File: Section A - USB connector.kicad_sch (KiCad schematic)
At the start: 5 parts, among them J2 USB4135-GF-A_REVA

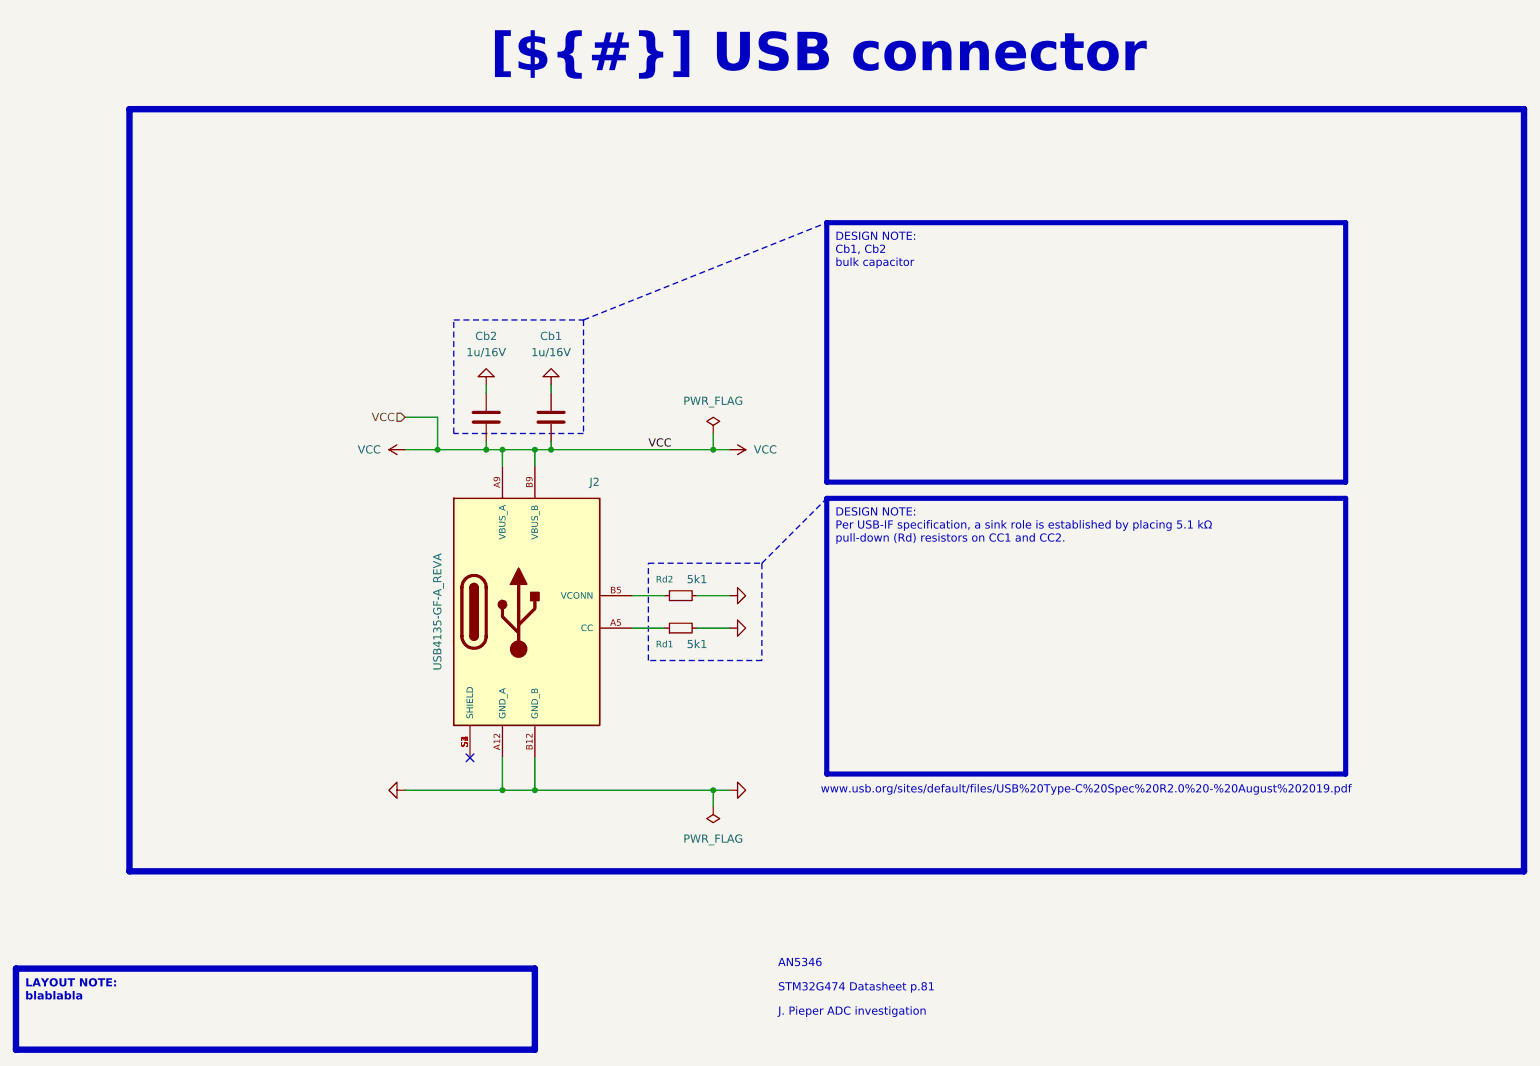
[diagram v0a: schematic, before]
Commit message: [CFG] Configuration update, added bom information fields
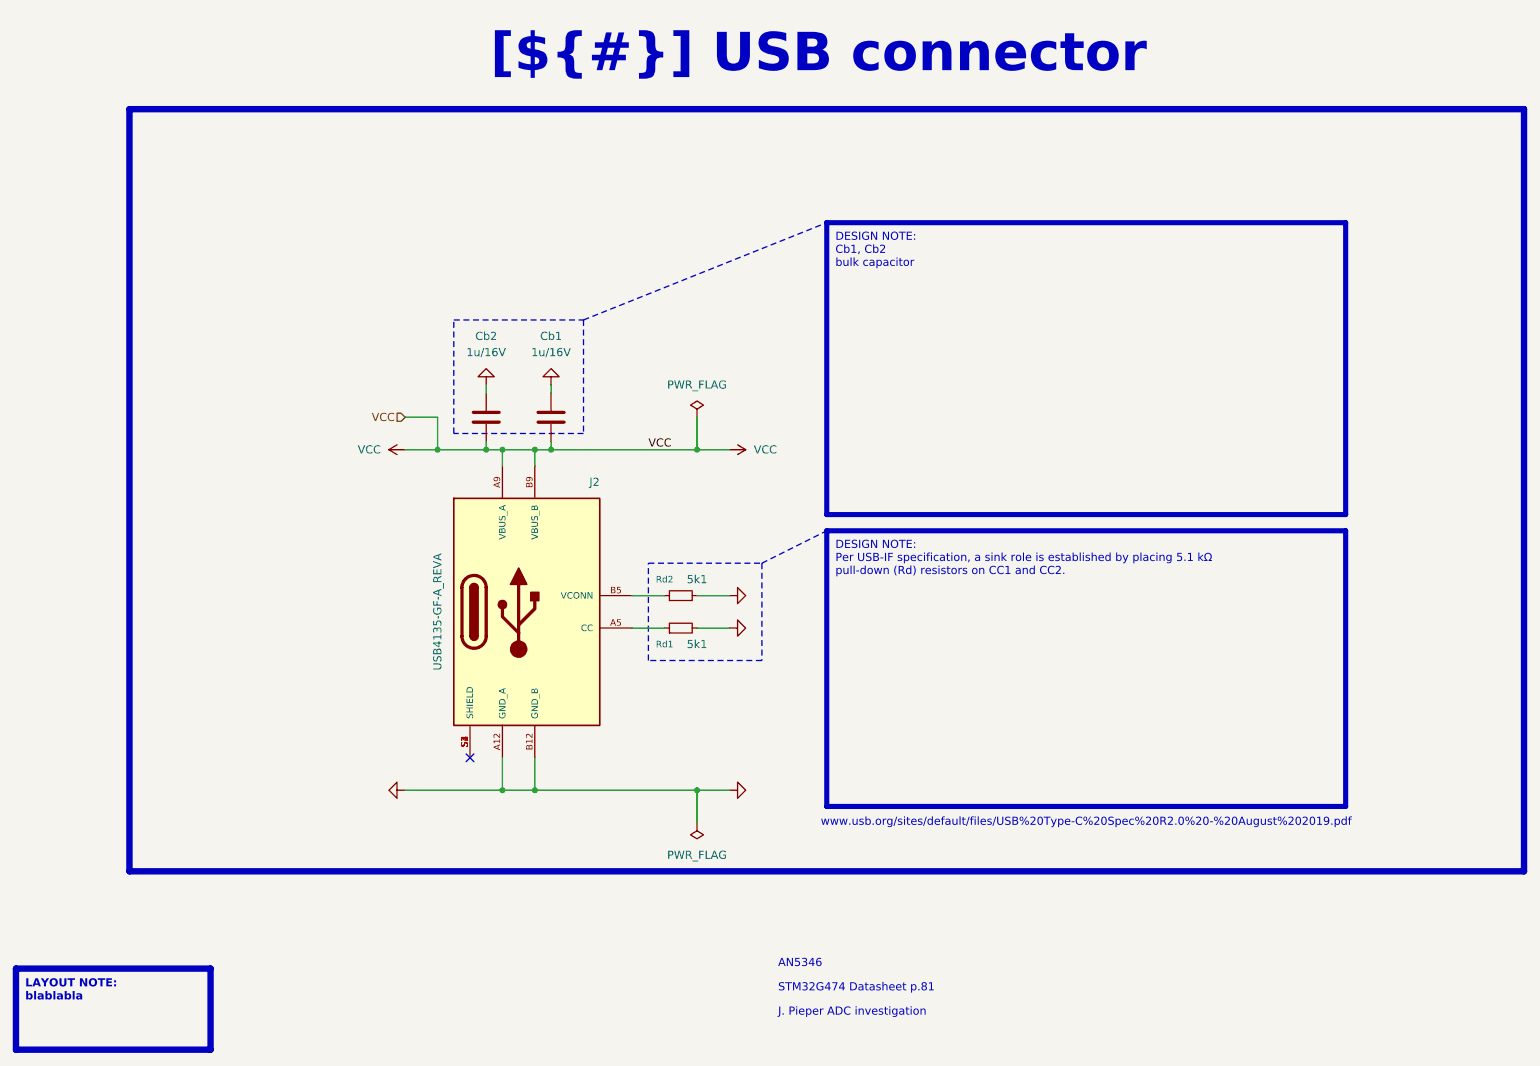
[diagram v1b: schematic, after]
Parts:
- Cb1, Cb2: BOM_INFO (none) -> TME have; BOM_STATUS (none) -> OK

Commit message: bom update, qr-code added
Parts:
- Cb1, Cb2: BOM_INFO TME have -> TME BOX
- J2: BOM_INFO (none) -> TME BOX; BOM_STATUS (none) -> OK
- Rd1, Rd2: BOM_INFO (none) -> TME BOX 25.06.2025; BOM_STATUS (none) -> OK
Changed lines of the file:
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@@
 			)
 		)
-		(property "BOM_INFO" ""
+		(property "BOM_INFO" "TME BOX 25.06.2025"
 			(at 127 104.14 90)
 			(effects
@@
 			)
 		)
-		(property "BOM_STATUS" ""
+		(property "BOM_STATUS" "OK"
 			(at 127 104.14 90)
 			(effects
@@
 			)
 		)
-		(property "BOM_INFO" "TME have"
+		(property "BOM_INFO" "TME BOX"
 			(at 106.68 76.2 0)
 			(effects
@@
 			)
 		)
-		(property "BOM_INFO" ""
+		(property "BOM_INFO" "TME BOX"
 			(at 101.6 106.68 0)
 			(effects
@@
 			)
 		)
-		(property "BOM_STATUS" ""
+		(property "BOM_STATUS" "OK"
 			(at 101.6 106.68 0)
 			(effects
@@
 			)
 		)
-		(property "BOM_INFO" "TME have"
+		(property "BOM_INFO" "TME BOX"
 			(at 96.52 76.2 0)
 			(effects
@@
 			)
 		)
-		(property "BOM_INFO" ""
+		(property "BOM_INFO" "TME BOX 25.06.2025"
 			(at 127 109.22 90)
 			(effects
@@
 			)
 		)
-		(property "BOM_STATUS" ""
+		(property "BOM_STATUS" "OK"
 			(at 127 109.22 90)
 			(effects

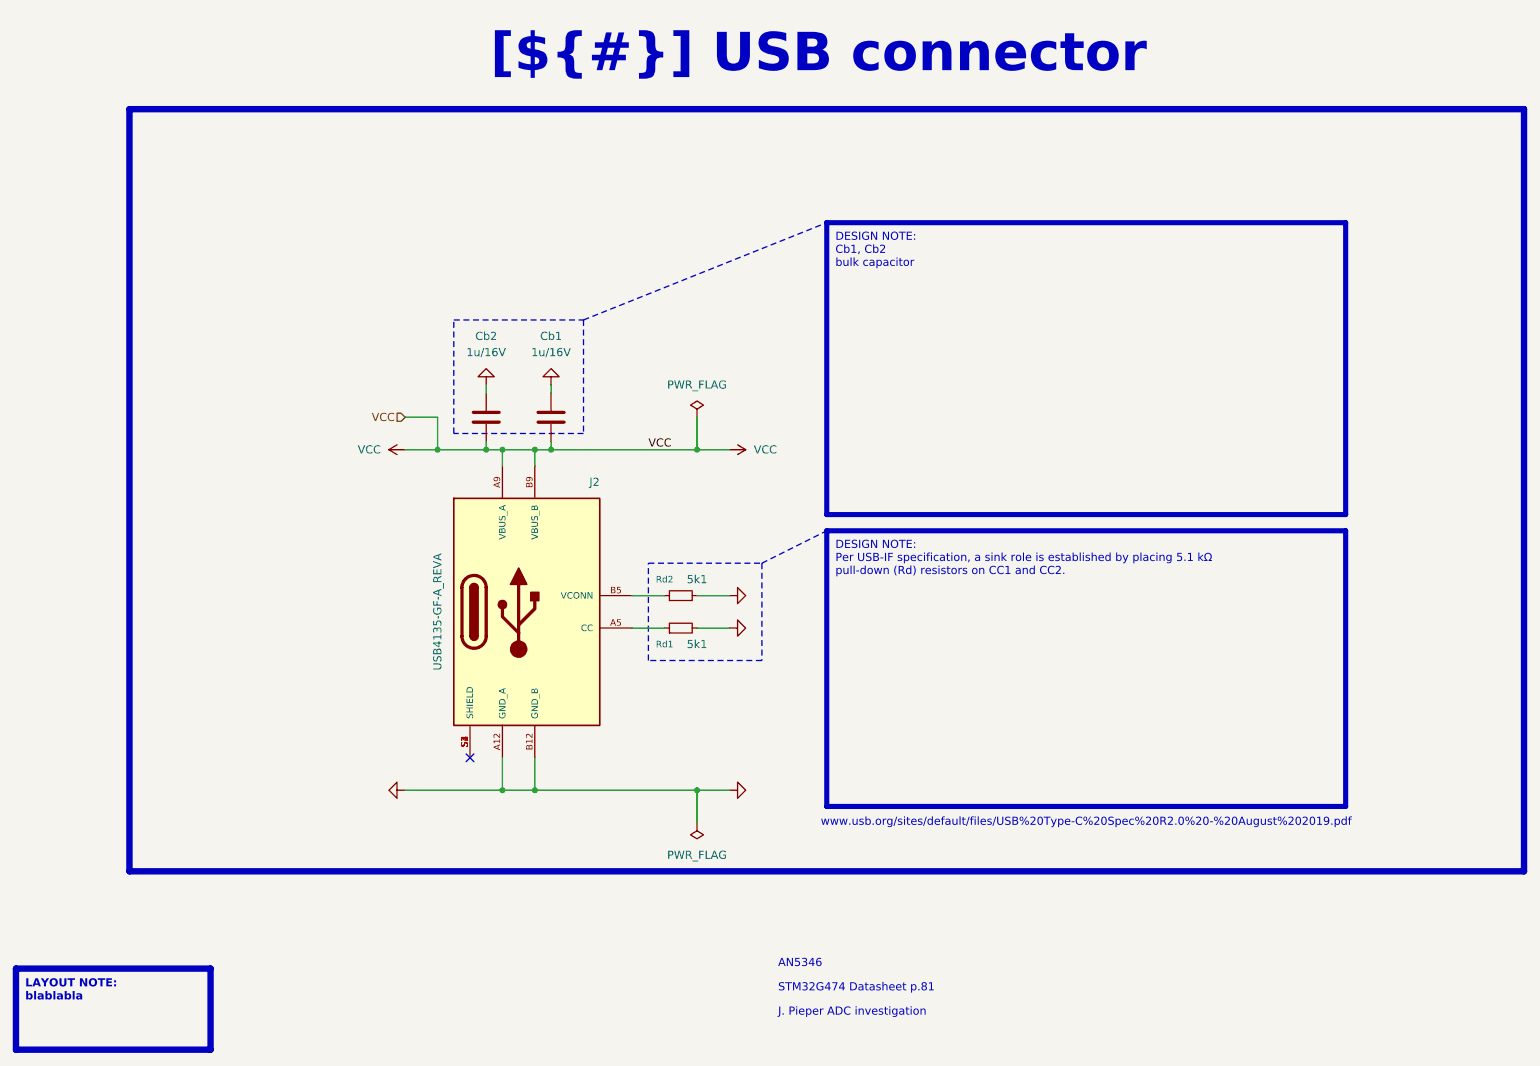
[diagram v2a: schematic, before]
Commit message: documentation update / block diagram
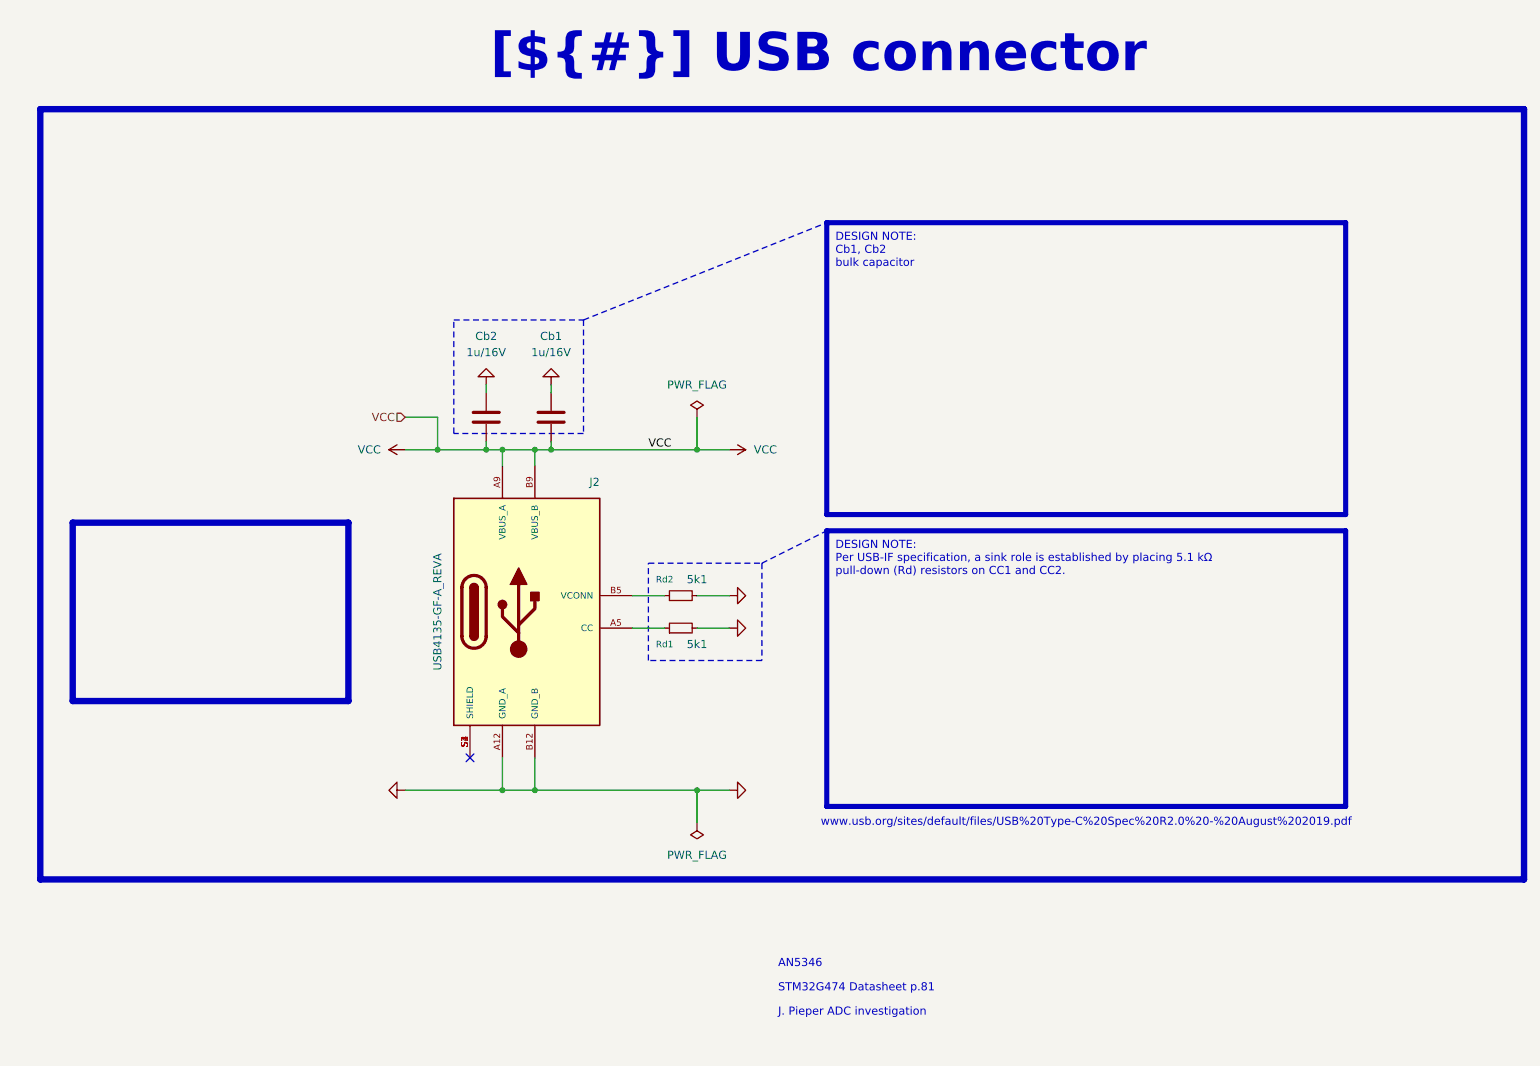
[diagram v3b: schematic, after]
